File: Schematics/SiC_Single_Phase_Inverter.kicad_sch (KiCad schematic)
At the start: 2 parts, among them J1 23AH8785-Black, J2 23AH8786-Red

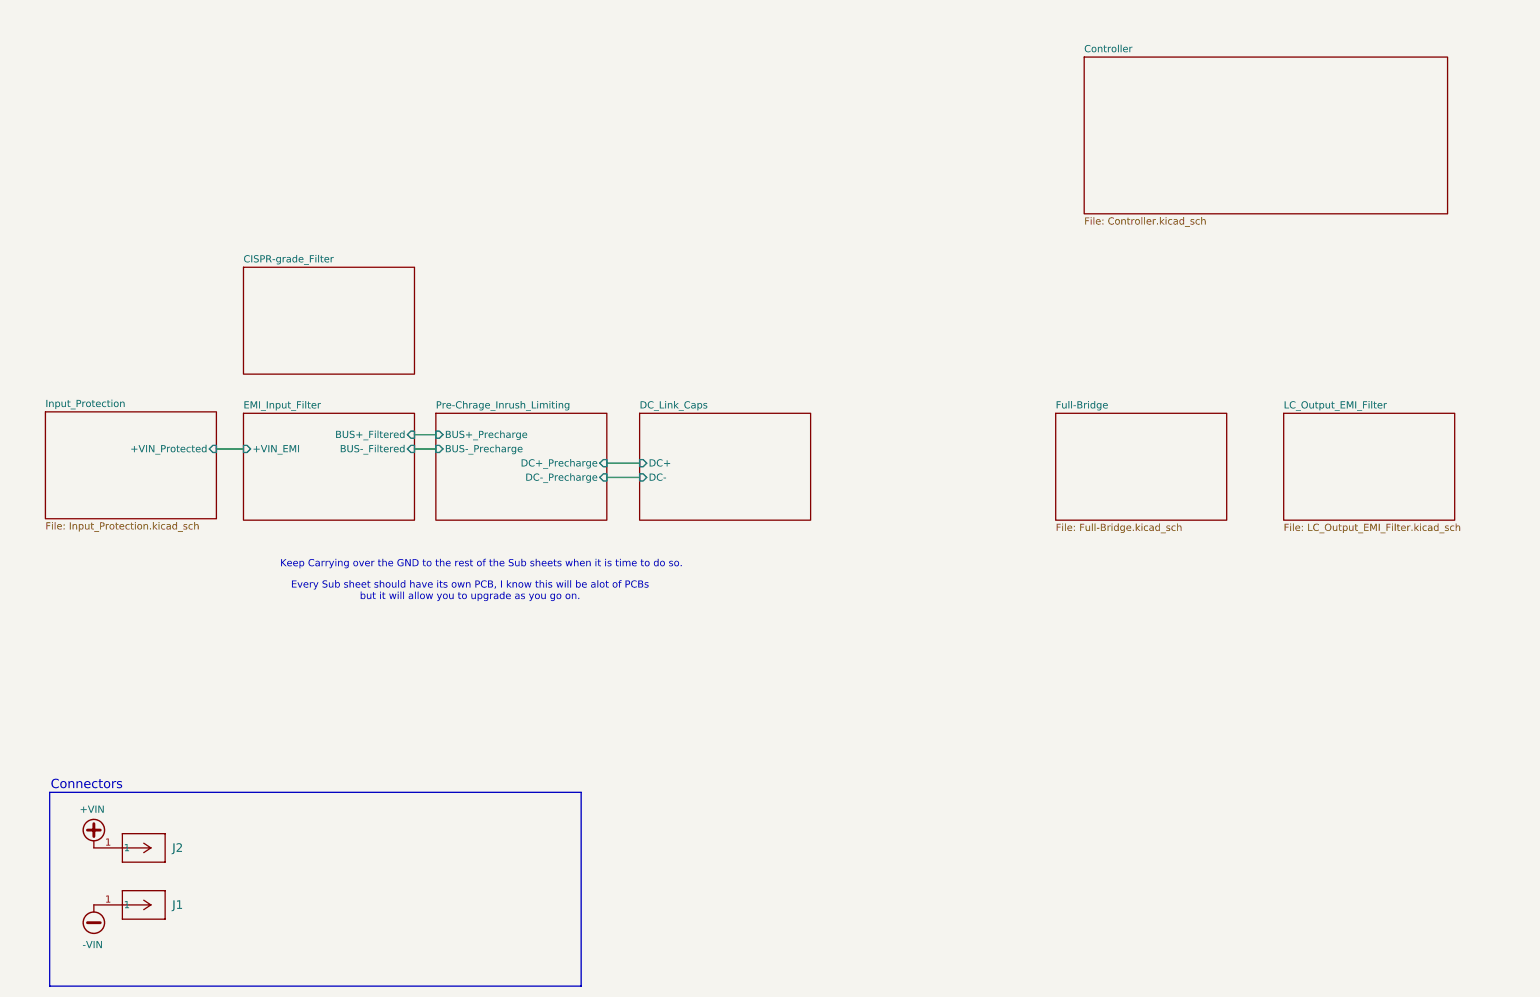
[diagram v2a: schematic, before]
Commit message: [WIP - SIC Inverter]
- Added 3d models for 3 parts
- Added 3 new footprints for the 3 added parts
- Changed footprint 23AH8785 and 86 Black and Red
- Finished WIP with EMI, Input Protection, and Precharge
- Added datasheet
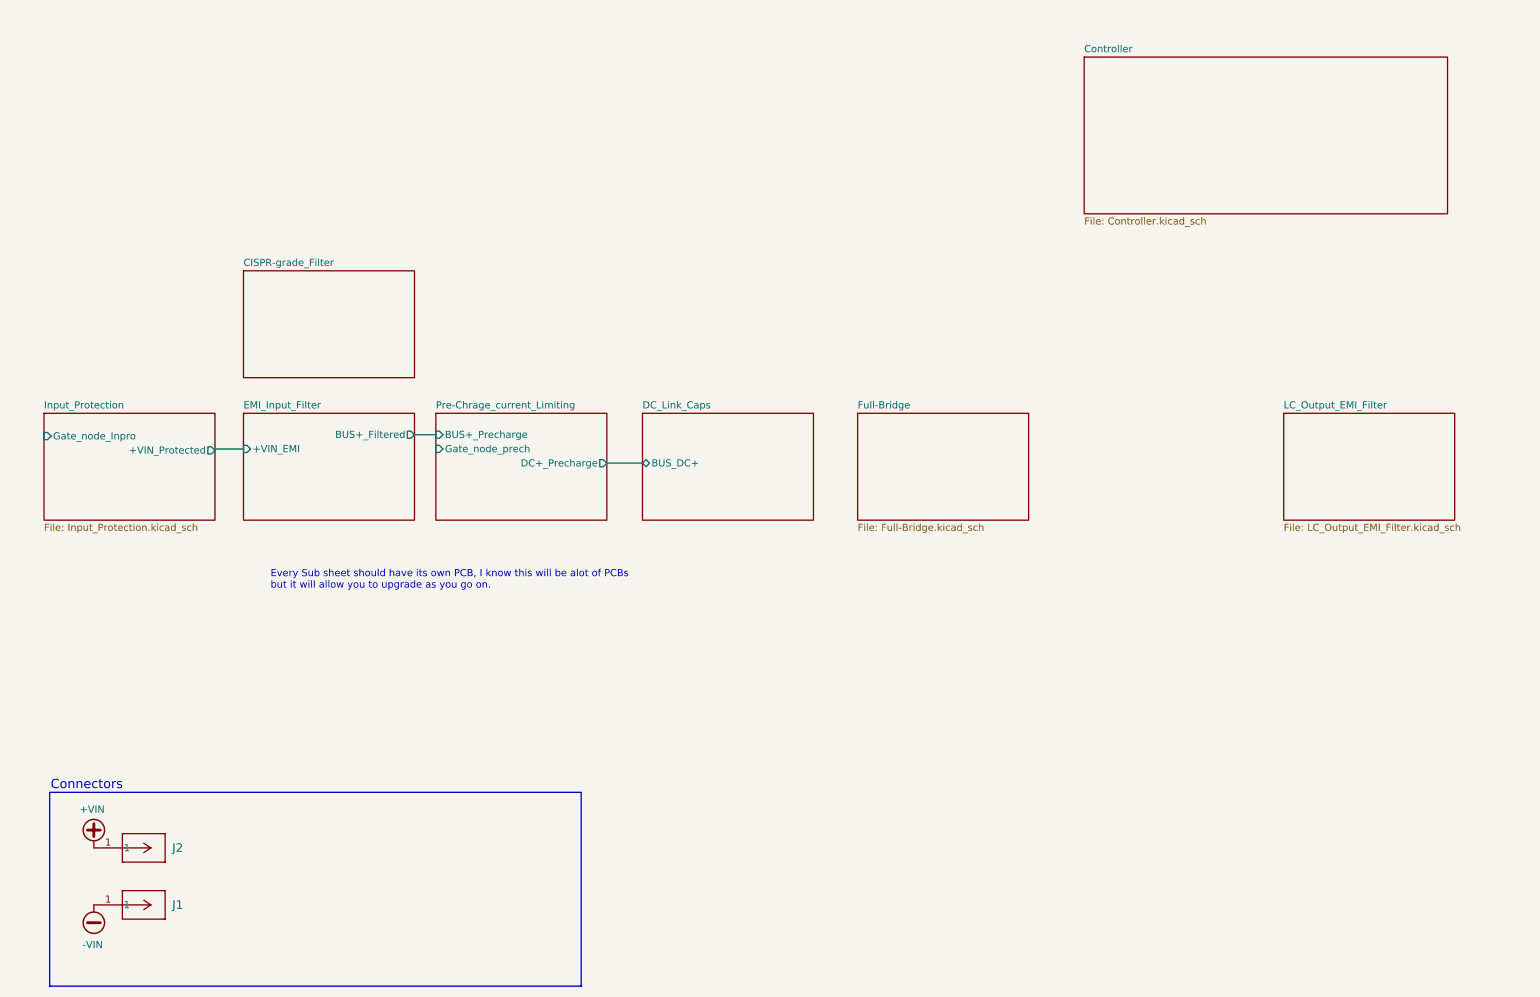
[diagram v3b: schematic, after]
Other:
- sheet Pre-Chrage_Inrush_Limiting renamed Pre-Chrage_current_Limiting
- sheet DC_Link_Caps ports: added BUS_DC+; removed DC+, DC-
- sheet EMI_Input_Filter ports: added none; removed BUS-_Filtered
- sheet Input_Protection ports: added Gate_node_Inpro; removed none
- sheet Pre-Chrage_current_Limiting ports: added Gate_node_prech; removed BUS-_Precharge, DC-_Precharge
- note removed: "Keep Carrying over the GND to the rest of the Sub sheets when it is time to do so."
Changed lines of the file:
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@@
 	(text "Every Sub sheet should have its own PCB, I know this will be alot of PCBs\nbut it will allow you to upgrade as you go on.\n"
 		(exclude_from_sim no)
-		(at 101.346 116.84 0)
+		(at 65.786 114.808 0)
 		(effects
 			(font
 				(size 1.27 1.27)
 			)
-		)
-	)
-	(text "Keep Carrying over the GND to the rest of the Sub sheets when it is time to do so. \n"
-		(exclude_from_sim no)
-		(at 103.378 112.014 0)
-		(effects
-			(font
-				(size 1.27 1.27)
-			)
+			(justify left)
 		)
 	)
@@
 	(wire
 		(pts
-			(xy 125.73 93.98) (xy 131.572 93.98)
+			(xy 125.73 93.98) (xy 132.08 93.98)
 		)
 		(stroke
@@
 	(wire
 		(pts
-			(xy 56.134 91.44) (xy 60.96 91.44)
-		)
-		(stroke
-			(width 0)
-			(type default)
-		)
-	)
-	(wire
-		(pts
-			(xy 91.44 91.44) (xy 95.25 91.44)
-		)
-		(stroke
-			(width 0)
-			(type default)
-		)
-	)
-	(wire
-		(pts
-			(xy 125.73 96.52) (xy 131.572 96.52)
+			(xy 55.88 91.44) (xy 60.96 91.44)
 		)
 		(stroke
@@
 			(color 0 0 0 0.0000)
 		)
-		(property "Sheetname" "Pre-Chrage_Inrush_Limiting"
+		(property "Sheetname" "Pre-Chrage_current_Limiting"
 			(at 95.25 84.3784 0)
 			(effects
@@
 			)
 		)
-		(pin "BUS-_Precharge" input
+		(pin "DC+_Precharge" output
+			(at 125.73 93.98 0)
+			(effects
+				(font
+					(size 1.27 1.27)
+				)
+				(justify right)
+			)
+		)
+		(pin "Gate_node_prech" input
 			(at 95.25 91.44 180)
 			(effects
@@
 				)
 				(justify left)
-			)
-		)
-		(pin "DC+_Precharge" input
-			(at 125.73 93.98 0)
-			(effects
-				(font
-					(size 1.27 1.27)
-				)
-				(justify right)
-			)
-		)
-		(pin "DC-_Precharge" input
-			(at 125.73 96.52 0)
-			(effects
-				(font
-					(size 1.27 1.27)
-				)
-				(justify right)
 			)
 		)
@@
 			)
 		)
-		(pin "BUS+_Filtered" input
+		(pin "BUS+_Filtered" output
 			(at 91.44 88.9 0)
-			(effects
-				(font
-					(size 1.27 1.27)
-				)
-				(justify right)
-			)
-		)
-		(pin "BUS-_Filtered" input
-			(at 91.44 91.44 0)
 			(effects
 				(font
@@
 	)
 	(sheet
-		(at 60.96 59.055)
+		(at 60.96 59.69)
 		(size 30.48 19.05)
 		(exclude_from_sim no)
@@
 		)
 		(property "Sheetname" "CISPR‑grade_Filter"
-			(at 60.96 58.3434 0)
+			(at 60.96 58.9784 0)
 			(effects
 				(font
@@
 		)
 		(property "Sheetfile" "CISPR‑grade_Filter.kicad_sch"
-			(at 60.96 78.6896 0)
+			(at 60.96 79.3246 0)
 			(effects
 				(font
@@
 	)
 	(sheet
-		(at 131.572 85.09)
+		(at 132.08 85.09)
 		(size 30.48 19.05)
 		(exclude_from_sim no)
@@
 		)
 		(property "Sheetname" "DC_Link_Caps"
-			(at 131.572 84.3784 0)
+			(at 132.08 84.3784 0)
 			(effects
 				(font
@@
 		)
 		(property "Sheetfile" "DC_Link_Caps.kicad_sch"
-			(at 131.572 104.7246 0)
+			(at 132.08 104.7246 0)
 			(effects
 				(font
@@
 			)
 		)
-		(pin "DC+" input
-			(at 131.572 93.98 180)
+		(pin "BUS_DC+" bidirectional
+			(at 132.08 93.98 180)
 			(effects
 				(font
@@
 			)
 		)
-		(pin "DC-" input
-			(at 131.572 96.52 180)
-			(effects
-				(font
-					(size 1.27 1.27)
-				)
-				(justify left)
-			)
-		)
 		(instances
 			(project "SiC_Single_Phase_Inverter"
@@
 	)
 	(sheet
-		(at 205.74 85.09)
+		(at 170.434 85.09)
 		(size 30.48 19.05)
 		(exclude_from_sim no)
@@
 		)
 		(property "Sheetname" "Full-Bridge"
-			(at 205.74 84.3784 0)
+			(at 170.434 84.3784 0)
 			(effects
 				(font
@@
 		)
 		(property "Sheetfile" "Full-Bridge.kicad_sch"
-			(at 205.74 104.7246 0)
+			(at 170.434 104.7246 0)
 			(effects
 				(font
@@
 	)
 	(sheet
-		(at 25.654 84.836)
+		(at 25.4 85.09)
 		(size 30.48 19.05)
 		(exclude_from_sim no)
@@
 		)
 		(property "Sheetname" "Input_Protection"
-			(at 25.654 84.1244 0)
+			(at 25.4 84.3784 0)
 			(effects
 				(font
@@
 		)
 		(property "Sheetfile" "Input_Protection.kicad_sch"
-			(at 25.654 104.4706 0)
+			(at 25.4 104.7246 0)
 			(effects
 				(font
@@
 			)
 		)
-		(pin "+VIN_Protected" input
-			(at 56.134 91.44 0)
+		(pin "+VIN_Protected" output
+			(at 55.88 91.694 0)
 			(effects
 				(font
@@
 			)
 		)
+		(pin "Gate_node_Inpro" input
+			(at 25.4 89.154 180)
+			(effects
+				(font
+					(size 1.27 1.27)
+				)
+				(justify left)
+			)
+		)

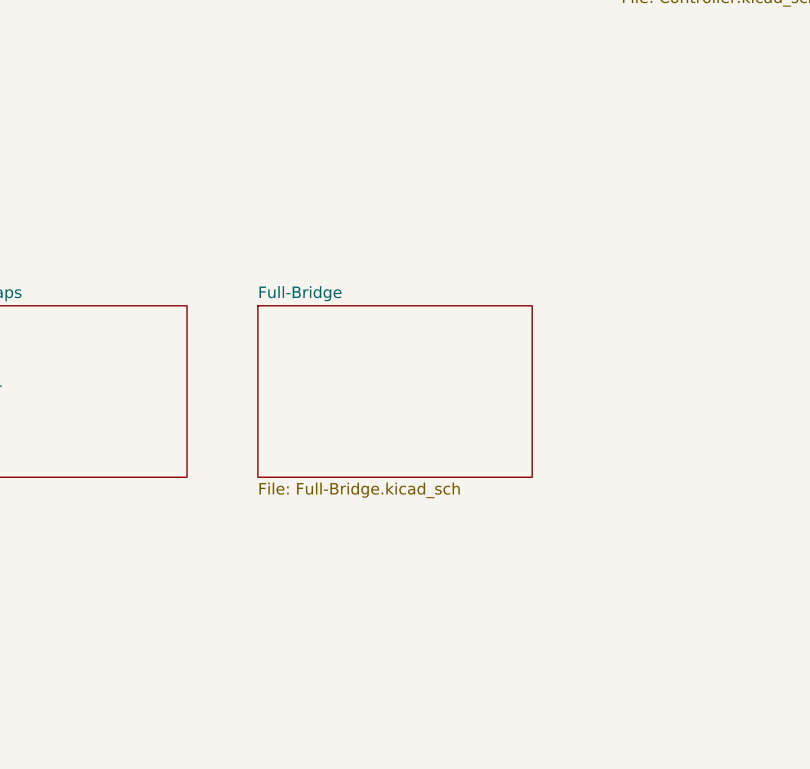
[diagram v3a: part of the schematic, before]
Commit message: Adding 100 pf caps to Leg A circuit, WIP texts
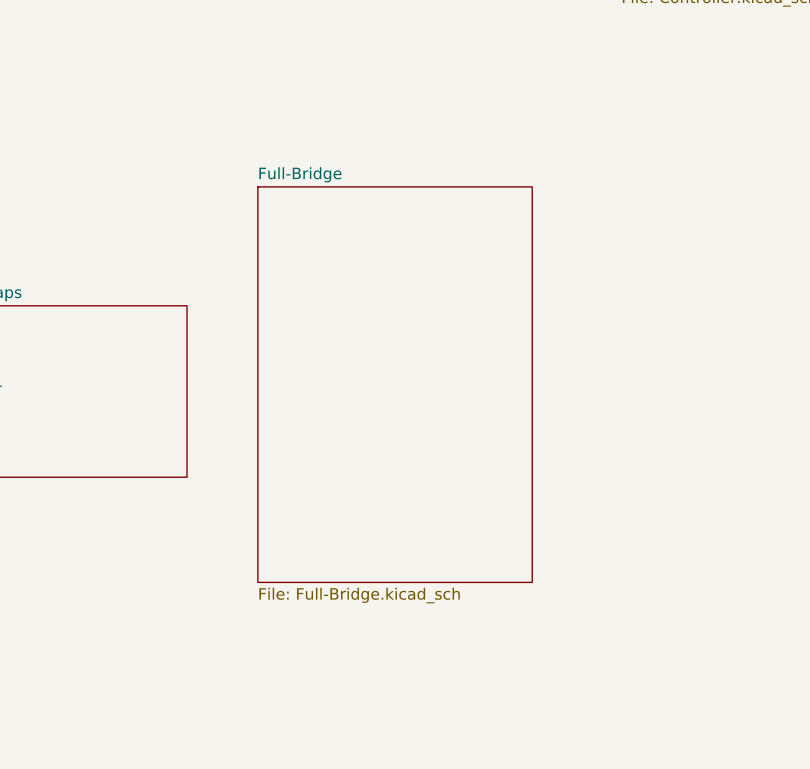
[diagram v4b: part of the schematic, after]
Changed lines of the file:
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@@
 	)
 	(sheet
-		(at 170.434 85.09)
-		(size 30.48 19.05)
+		(at 170.434 71.882)
+		(size 30.48 43.942)
 		(exclude_from_sim no)
 		(in_bom yes)
@@
 		)
 		(property "Sheetname" "Full-Bridge"
-			(at 170.434 84.3784 0)
+			(at 170.434 71.1704 0)
 			(effects
 				(font
@@
 		)
 		(property "Sheetfile" "Full-Bridge.kicad_sch"
-			(at 170.434 104.7246 0)
+			(at 170.434 116.4086 0)
 			(effects
 				(font

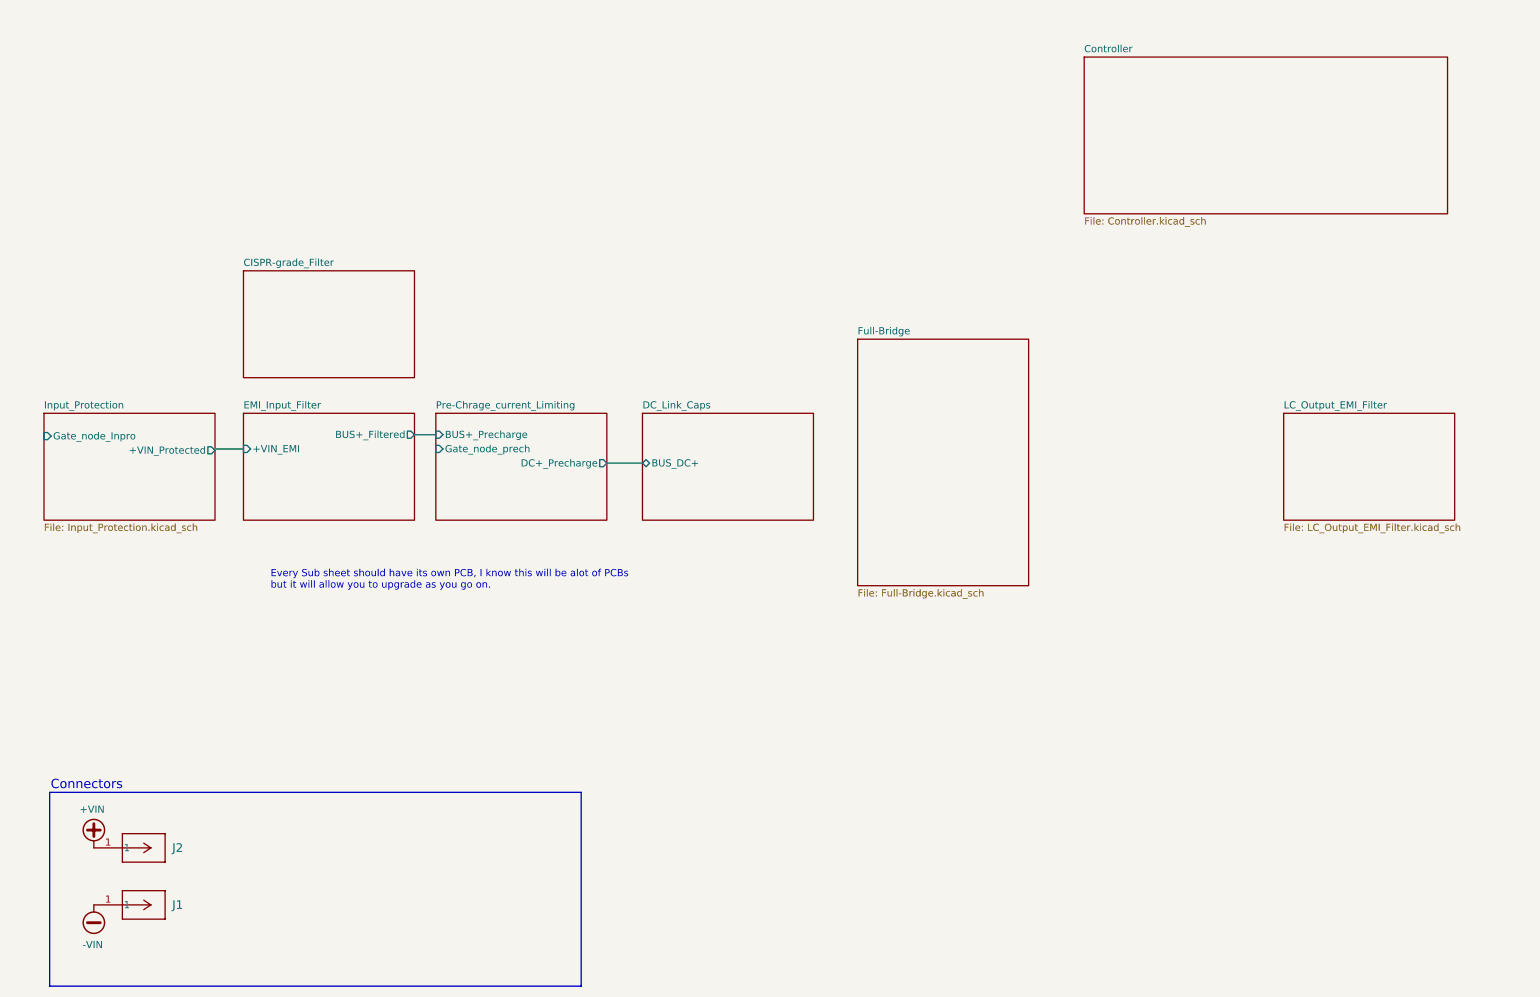
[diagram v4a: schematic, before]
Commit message: [WIP Full Bridge]
- Finished Leg B and cleaned up sub sheets Leg A and Leg B
- Added Hierarchical sheet pins for Leg A,B and Full Bridge
- Added power schamtic for future use
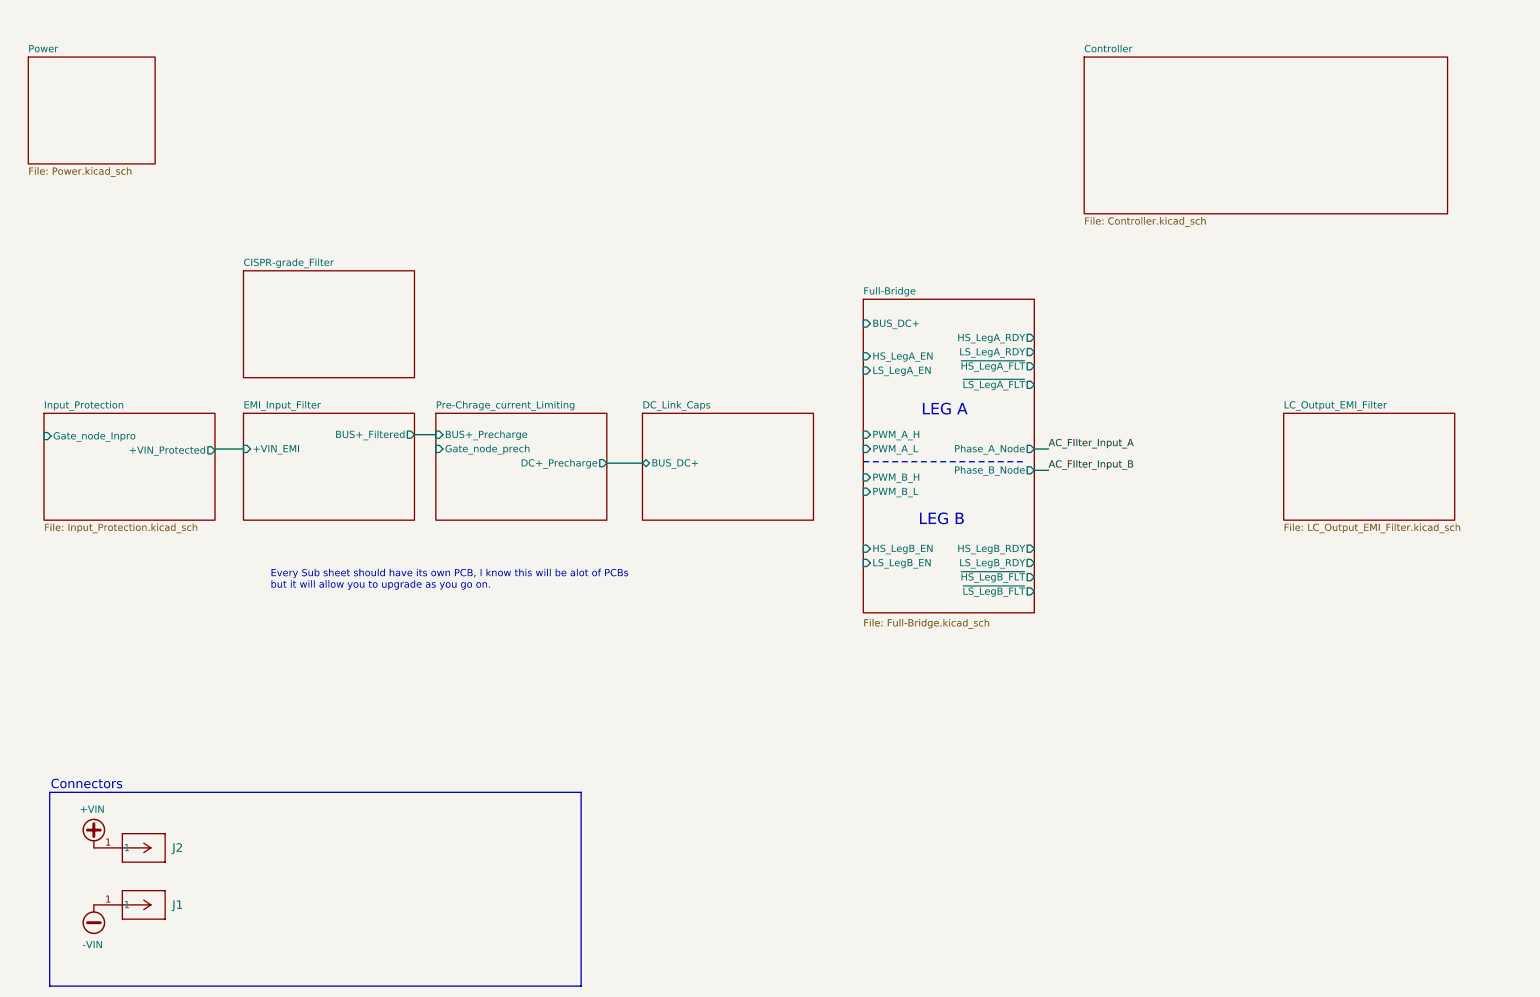
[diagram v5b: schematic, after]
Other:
- added sheet Power (Power.kicad_sch)
- sheet Full-Bridge ports: added BUS_DC+, HS_LegA_EN, HS_LegA_RDY, HS_LegB_EN, HS_LegB_RDY, LS_LegA_EN, LS_LegA_RDY, LS_LegB_EN, LS_LegB_RDY, PWM_A_H, PWM_A_L, PWM_B_H, PWM_B_L, Phase_A_Node, Phase_B_Node, ~{HS_LegA_FLT}, ~{HS_LegB_FLT}, ~{LS_LegA_FLT}, ~{LS_LegB_FLT}; removed none
- note added: "LEG A"
- note added: "LEG B"
